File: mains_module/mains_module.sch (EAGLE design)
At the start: 19 parts, among them Q1 IRF540, X1 22-23-2051

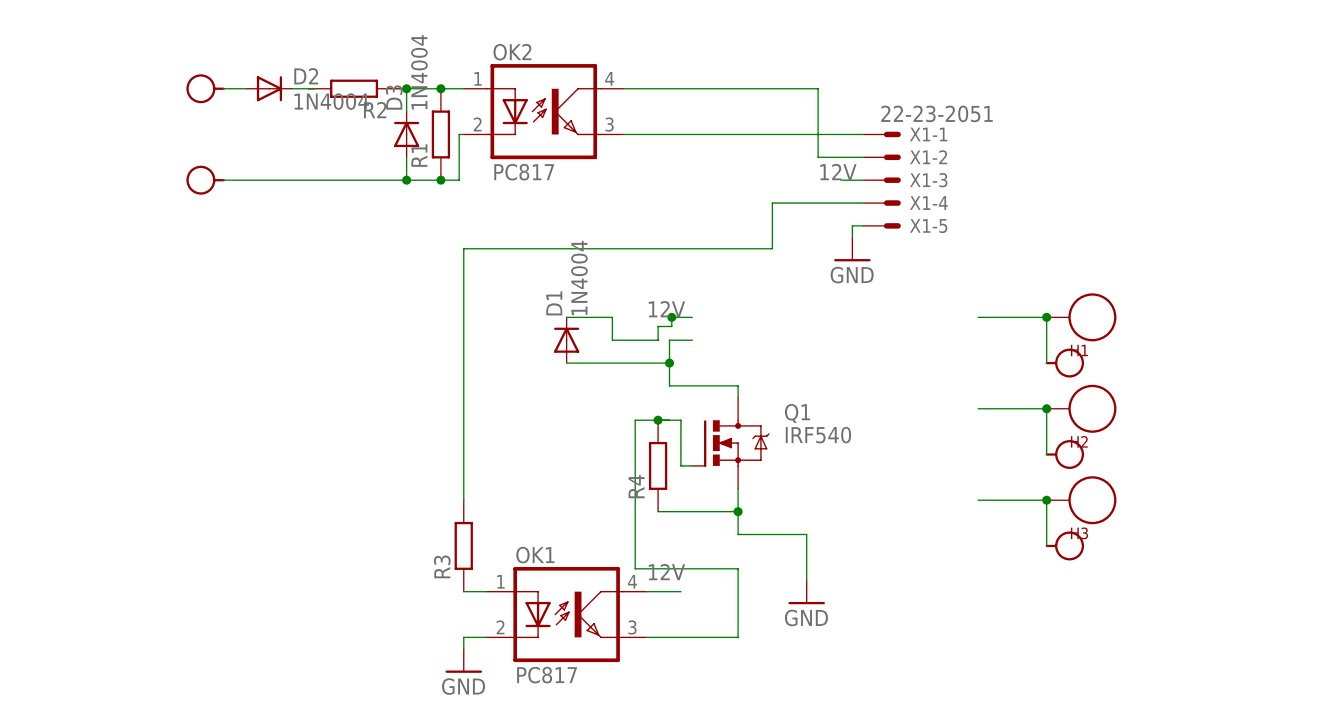
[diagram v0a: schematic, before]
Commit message: Completed T-type-relay eagle part, created schematic and board of mains_module, and updates to shopping list/expense list
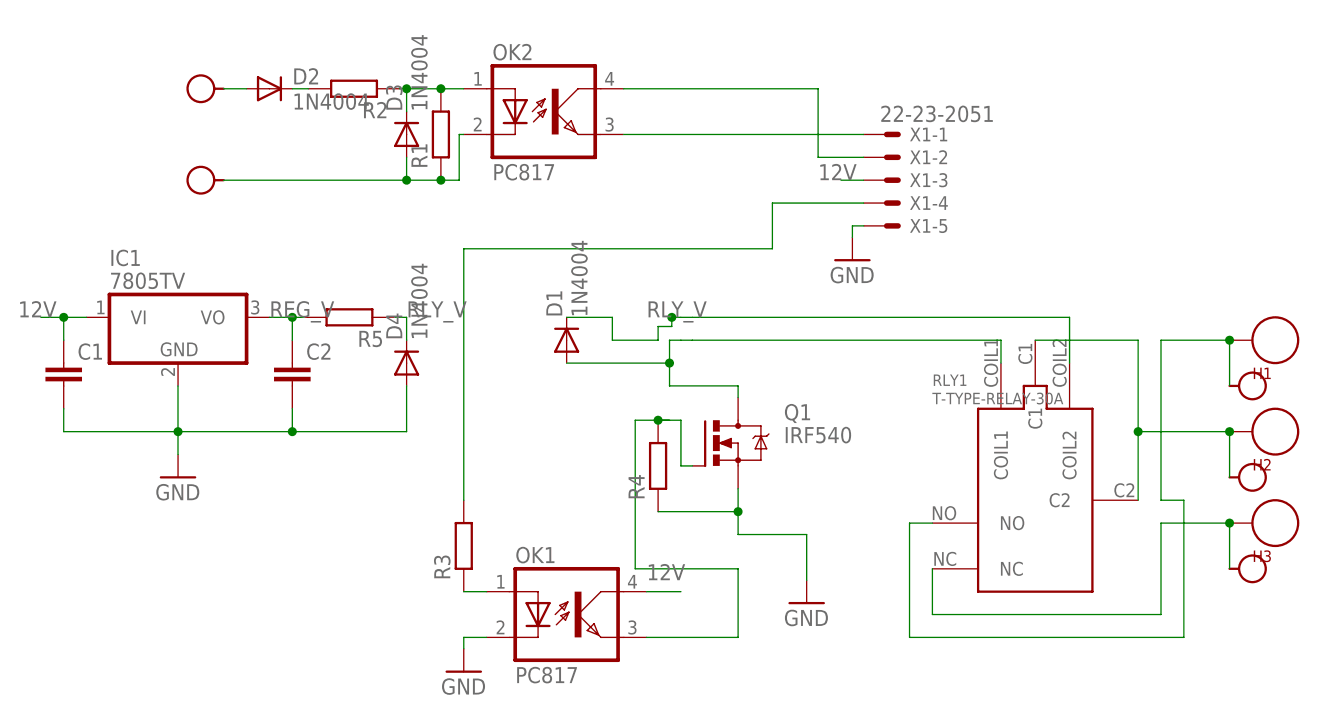
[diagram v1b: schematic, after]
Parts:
- added C1, C2: (no value), capacitor-wima:C2,5-3
- added D4: 1N4004, diode:1N4004
- added IC1: 7805TV, linear:7805TV
- added R5: (no value), rcl:R-EU_0207/7
- added RLY1: T-TYPE-RELAY-30A, T-type-relay:T-TYPE-RELAY-30A
- R1, R2, R3, R4: device resistor:R-EU_0204/5 -> rcl:R-EU_0207/7
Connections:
- removed net N$11: D2.C
- new net N$14: H2.P$1, H5.P$1, RLY1.C1, RLY1.C2
- new net REG_V: C2.1, IC1.VO, R5.2
- new net RLY_V: D1.C, D4.C, R5.1, RLY1.COIL2
- net 12V: now also C1.1, IC1.VI; no longer D1.C
- net GND: now also C1.2, C2.2, D4.A, IC1.GND
- net N$3: now also RLY1.NO
- net N$5: now also RLY1.COIL1
- net N$8: now also D2.C, R2.2; no longer H2.P$1, H5.P$1
- net N$9: now also RLY1.NC
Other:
- moved on the sheet: H1, H2, H3
